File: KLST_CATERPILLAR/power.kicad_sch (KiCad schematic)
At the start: 18 parts, among them Q1 AO3401A, Q4 AO3401A, U1 AMS1117-3.3, U14 AMS1117-1.8

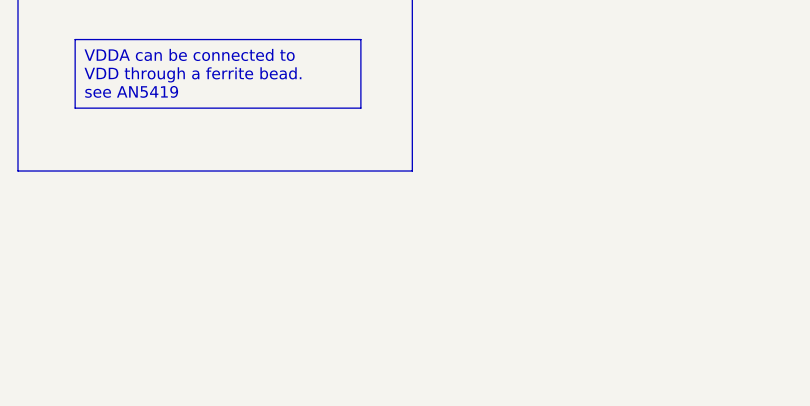
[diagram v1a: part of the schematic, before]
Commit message: fixed: connected 5V to USB power
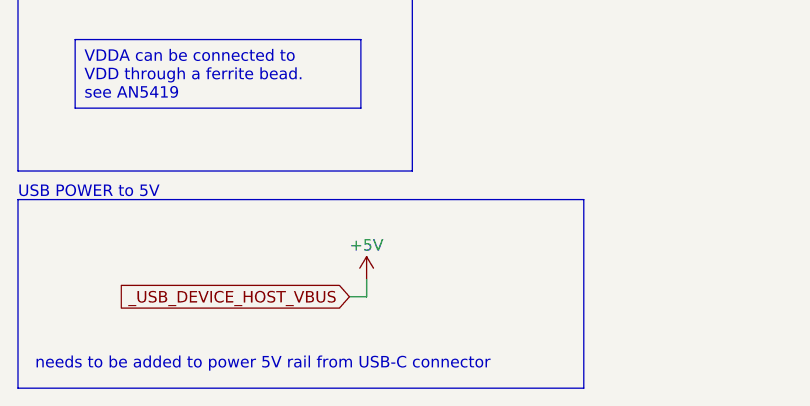
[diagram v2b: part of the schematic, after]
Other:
- note added: "USB POWER to 5V"
- note added: "needs to be added to power 5V rail from USB-C connector"
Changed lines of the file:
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@@
+	(wire
+		(pts
+			(xy 54.61 132.715) (xy 54.61 130.81)
+		)
+		(stroke
+			(width 0)
+			(type default)
+		)
+	)
 	(wire
 		(pts
@@
 		(pts
 			(xy 147.32 40.005) (xy 147.32 43.815)
+		)
+		(stroke
+			(width 0)
+			(type default)
+		)
+	)
+	(wire
+		(pts
+			(xy 52.705 132.715) (xy 54.61 132.715)
 		)
 		(stroke
@@
 		(start 192.405 16.51)
 		(end 261.62 37.465)
+		(stroke
+			(width 0)
+			(type default)
+		)
+		(fill
+			(type none)
+		)
+	)
+	(rectangle
+		(start 15.875 121.92)
+		(end 78.74 142.875)
 		(stroke
 			(width 0)
@@
 		)
 	)
+	(text "USB POWER to 5V"
+		(exclude_from_sim no)
+		(at 15.875 121.92 0)
+		(effects
+			(font
+				(size 1.27 1.27)
+			)
+			(justify left bottom)
+		)
+	)
 	(text "@NOTE(200mA rating)"
 		(exclude_from_sim no)
@@
 		(exclude_from_sim no)
 		(at 16.002 16.51 0)
+		(effects
+			(font
+				(size 1.27 1.27)
+			)
+			(justify left bottom)
+		)
+	)
+	(text "needs to be added to power 5V rail from USB-C connector"
+		(exclude_from_sim no)
+		(at 17.78 140.97 0)
 		(effects
 			(font
@@
 		)
 	)
+	(global_label "_USB_DEVICE_HOST_VBUS"
+		(shape input)
+		(at 52.705 132.715 180)
+		(fields_autoplaced yes)
+		(effects
+			(font
+				(size 1.27 1.27)
+			)
+			(justify right)
+		)
+		(property "Intersheetrefs" "${INTERSHEET_REFS}"
+			(at 25.8507 132.715 0)
+			(effects
+				(font
+					(size 1.27 1.27)
+				)
+				(justify right)
+				(hide yes)
+			)
+		)
+	)
 	(symbol
 		(lib_id "power:PWR_FLAG")
@@
 					(unit 1)
 				)
+			)
+		)
+	)
+	(symbol
+		(lib_id "power:+5V")
+		(at 54.61 130.81 0)
+		(unit 1)
+		(exclude_from_sim no)
+		(in_bom yes)
+		(on_board yes)
+		(dnp no)
+		(property "Reference" "#PWR049"
+			(at 54.61 134.62 0)
+			(effects
+				(font
+					(size 1.27 1.27)
+				)
+				(hide yes)
+			)
+		)
+		(property "Value" "+5V"
+			(at 54.61 127 0)
+			(effects
+				(font
+					(size 1.27 1.27)
+				)
+			)
+		)
+		(property "Footprint" ""
+			(at 54.61 130.81 0)
+			(effects
+				(font
+					(size 1.27 1.27)
+				)
+				(hide yes)
+			)
+		)
+		(property "Datasheet" ""
+			(at 54.61 130.81 0)
+			(effects
+				(font
+					(size 1.27 1.27)
+				)
+				(hide yes)
+			)
+		)
+		(property "Description" ""
+			(at 54.61 130.81 0)
+			(effects
+				(font
+					(size 1.27 1.27)
+				)
+				(hide yes)
+			)
+		)
+		(pin "1"
+		)
+		(instances
+			(project "KLST_CATERPILLAR"
+				(path "/b4513875-4c57-4720-bcc5-43ead67fe18f/efc23d99-04cc-4530-a8d8-9c096b510f30"
+					(reference "#PWR049")
+					(unit 1)
+				)

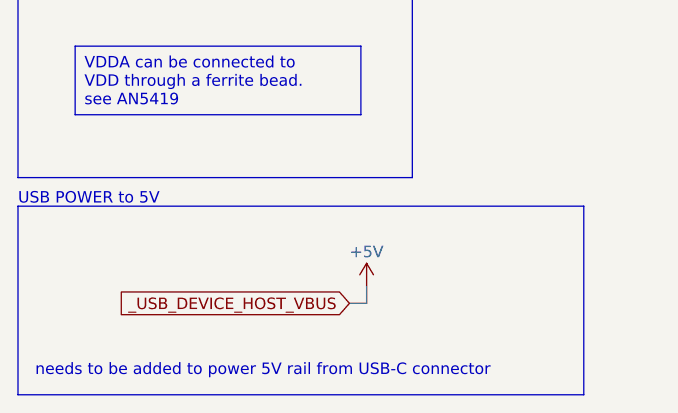
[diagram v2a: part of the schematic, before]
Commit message: added net tie for USB to 5V
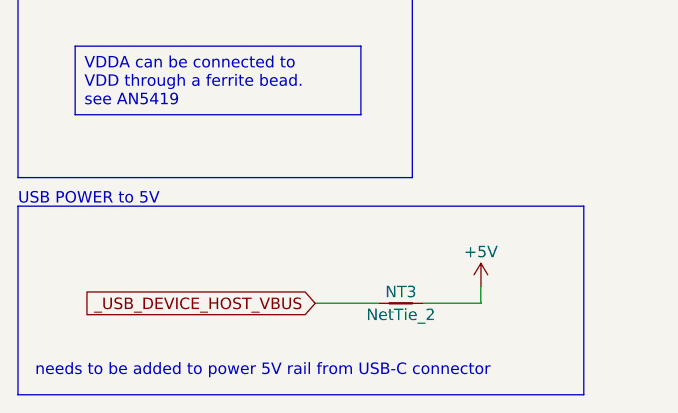
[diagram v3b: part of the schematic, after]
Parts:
- added NT3: NetTie_2, NetTie:NetTie-2_SMD_Pad2.0mm, symbol Device:NetTie_2
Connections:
- net +5V: now also NT3.2
- new net _USB_DEVICE_HOST_VBUS: NT3.1
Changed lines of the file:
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@@
 	(wire
 		(pts
-			(xy 54.61 132.715) (xy 54.61 130.81)
+			(xy 67.31 132.715) (xy 67.31 130.81)
 		)
 		(stroke
@@
 	(wire
 		(pts
+			(xy 60.96 132.715) (xy 67.31 132.715)
+		)
+		(stroke
+			(width 0)
+			(type default)
+		)
+	)
+	(wire
+		(pts
 			(xy 62.865 40.005) (xy 65.405 40.005)
 		)
@@
 	(wire
 		(pts
-			(xy 52.705 132.715) (xy 54.61 132.715)
+			(xy 48.895 132.715) (xy 55.88 132.715)
 		)
 		(stroke
@@
 	(global_label "_USB_DEVICE_HOST_VBUS"
 		(shape input)
-		(at 52.705 132.715 180)
+		(at 48.895 132.715 180)
 		(fields_autoplaced yes)
 		(effects
@@
 		)
 		(property "Intersheetrefs" "${INTERSHEET_REFS}"
-			(at 25.8507 132.715 0)
+			(at 22.0407 132.715 0)
 			(effects
 				(font
@@
 	)
 	(symbol
+		(lib_id "Device:NetTie_2")
+		(at 58.42 132.715 0)
+		(mirror x)
+		(unit 1)
+		(exclude_from_sim no)
+		(in_bom no)
+		(on_board yes)
+		(dnp no)
+		(property "Reference" "NT3"
+			(at 58.42 131.445 0)
+			(effects
+				(font
+					(size 1.27 1.27)
+				)
+			)
+		)
+		(property "Value" "NetTie_2"
+			(at 58.42 133.985 0)
+			(effects
+				(font
+					(size 1.27 1.27)
+				)
+			)
+		)
+		(property "Footprint" "NetTie:NetTie-2_SMD_Pad2.0mm"
+			(at 58.42 132.715 0)
+			(effects
+				(font
+					(size 1.27 1.27)
+				)
+				(hide yes)
+			)
+		)
+		(property "Datasheet" "~"
+			(at 58.42 132.715 0)
+			(effects
+				(font
+					(size 1.27 1.27)
+				)
+				(hide yes)
+			)
+		)
+		(property "Description" ""
+			(at 58.42 132.715 0)
+			(effects
+				(font
+					(size 1.27 1.27)
+				)
+				(hide yes)
+			)
+		)
+		(property "JLCPCB" "DNF"
+			(at 58.42 132.715 0)
+			(effects
+				(font
+					(size 1.27 1.27)
+				)
+				(hide yes)
+			)
+		)
+		(pin "1"
+		)
+		(pin "2"
+		)
+		(instances
+			(project "KLST_CATERPILLAR"
+				(path "/b4513875-4c57-4720-bcc5-43ead67fe18f/efc23d99-04cc-4530-a8d8-9c096b510f30"
+					(reference "NT3")
+					(unit 1)
+				)
+			)
+		)
+	)
+	(symbol
 		(lib_name "+5V_1")
 		(lib_id "power:+5V")
@@
 	(symbol
 		(lib_id "power:+5V")
-		(at 54.61 130.81 0)
+		(at 67.31 130.81 0)
 		(unit 1)
 		(exclude_from_sim no)
@@
 		(dnp no)
 		(property "Reference" "#PWR049"
-			(at 54.61 134.62 0)
+			(at 67.31 134.62 0)
 			(effects
 				(font
@@
 		)
 		(property "Value" "+5V"
-			(at 54.61 127 0)
+			(at 67.31 127 0)
 			(effects
 				(font
@@
 		)
 		(property "Footprint" ""
-			(at 54.61 130.81 0)
+			(at 67.31 130.81 0)
 			(effects
 				(font
@@
 		)
 		(property "Datasheet" ""
-			(at 54.61 130.81 0)
+			(at 67.31 130.81 0)
 			(effects
 				(font
@@
 		)
 		(property "Description" ""
-			(at 54.61 130.81 0)
-			(effects
-				(font
+			(at 67.31 130.81 0)
+			(effects
+				(font

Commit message: added net tie for USB to 5V
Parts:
- NT3: footprint NetTie:NetTie-2_SMD_Pad2.0mm -> NetTie:NetTie-2_SMD_Pad0.5mm
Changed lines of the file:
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@@
 			)
 		)
-		(property "Footprint" "NetTie:NetTie-2_SMD_Pad2.0mm"
+		(property "Footprint" "NetTie:NetTie-2_SMD_Pad0.5mm"
 			(at 58.42 132.715 0)
 			(effects
